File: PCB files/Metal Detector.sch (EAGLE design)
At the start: 125 parts, among them IC1 NE5534AD, IC2 BQ24133RGYR, IC3 LM317MBSTT3, IC4 ESP32-WROOM-32UE-N4, IC5 CP2102, IC6 LM317MBSTT3, J1 L-KLS1-TSJ3.5-013, J2/BATTERY DG128-5.0-02P-14, Q1 IRF740, Q2 BC556, Q3 SI2312CDS-T1-GE3, Q4 MBT3904DW1T1, Q5 SI2312CDS-T1-GE3, Q6 SI2323CDS-T1-GE3, Q7 BC847AE6327HTSA1, T1 BC547, X1 A1944-50, X2 DC21MMX

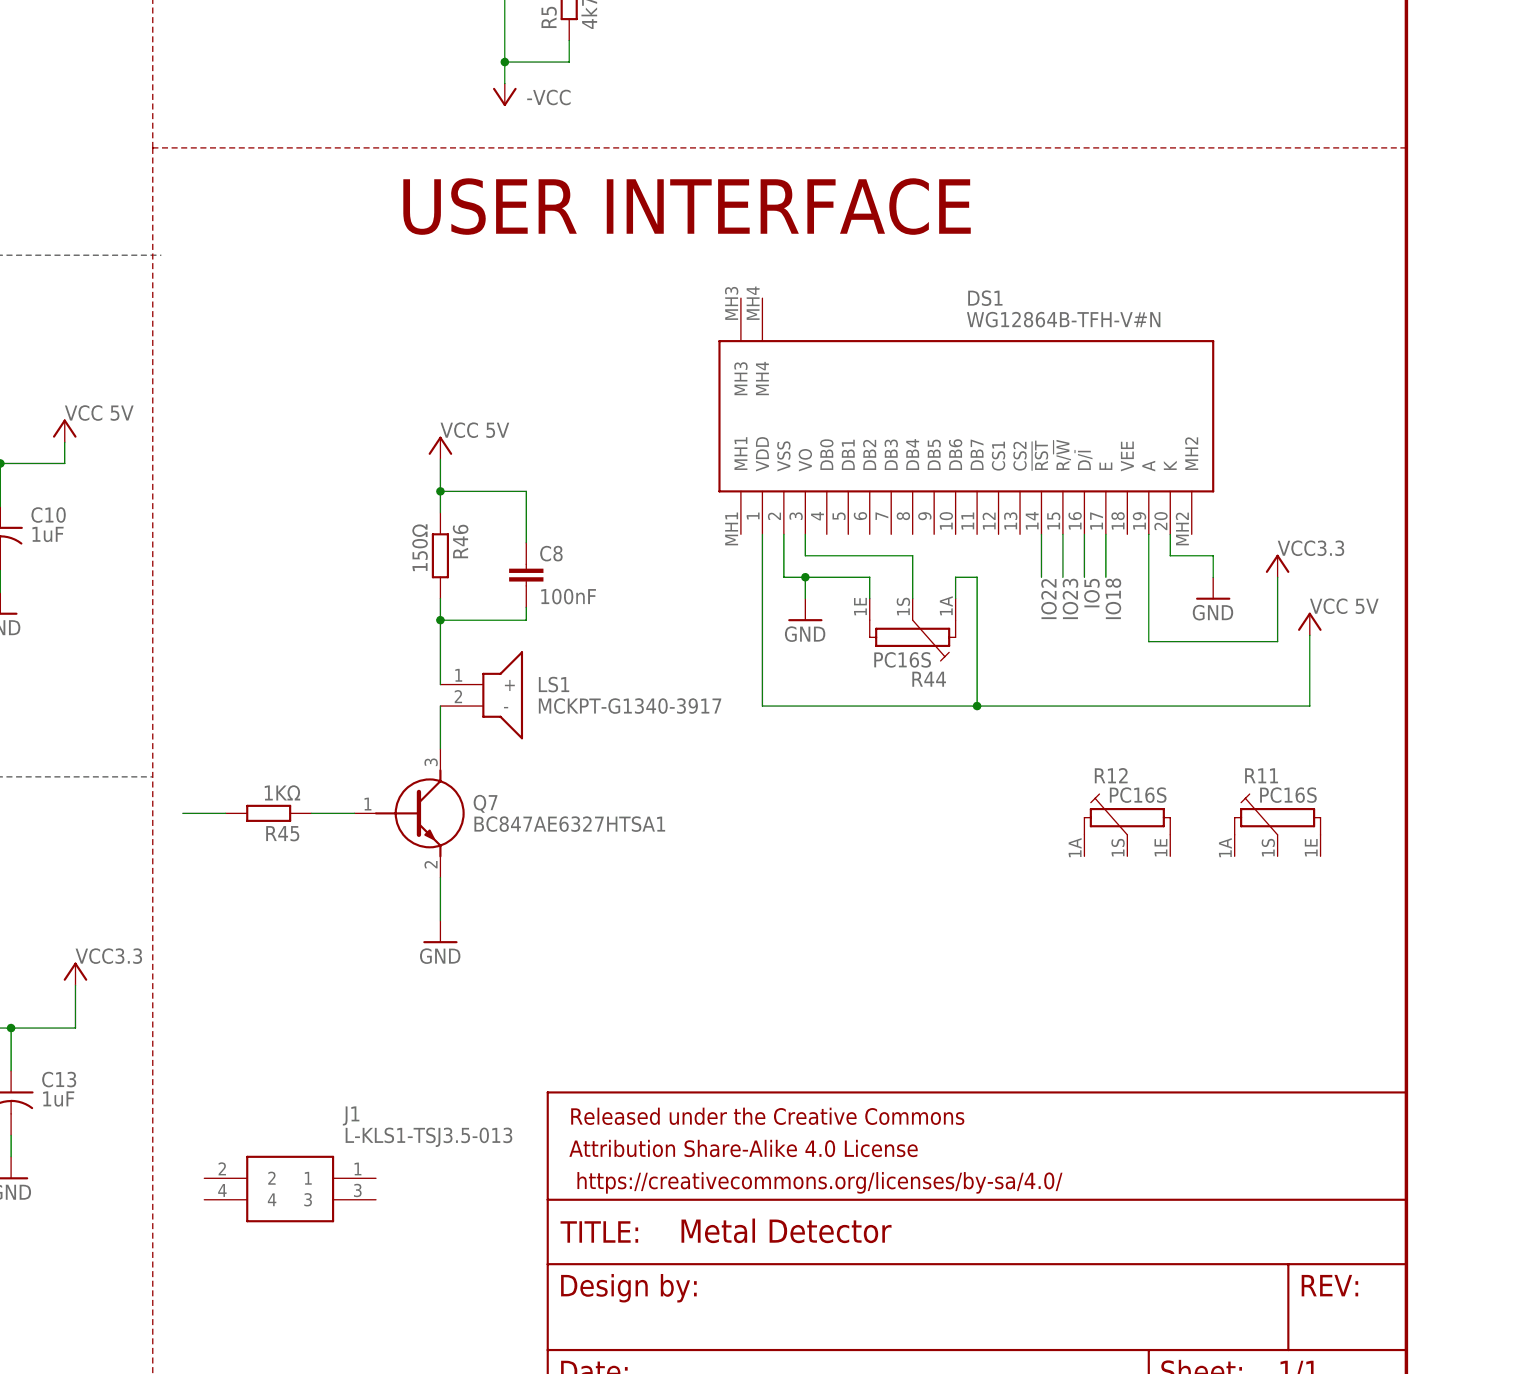
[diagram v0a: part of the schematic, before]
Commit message: Add files via upload
Connected and added Spekers, volume and sensitivty connections with MCU
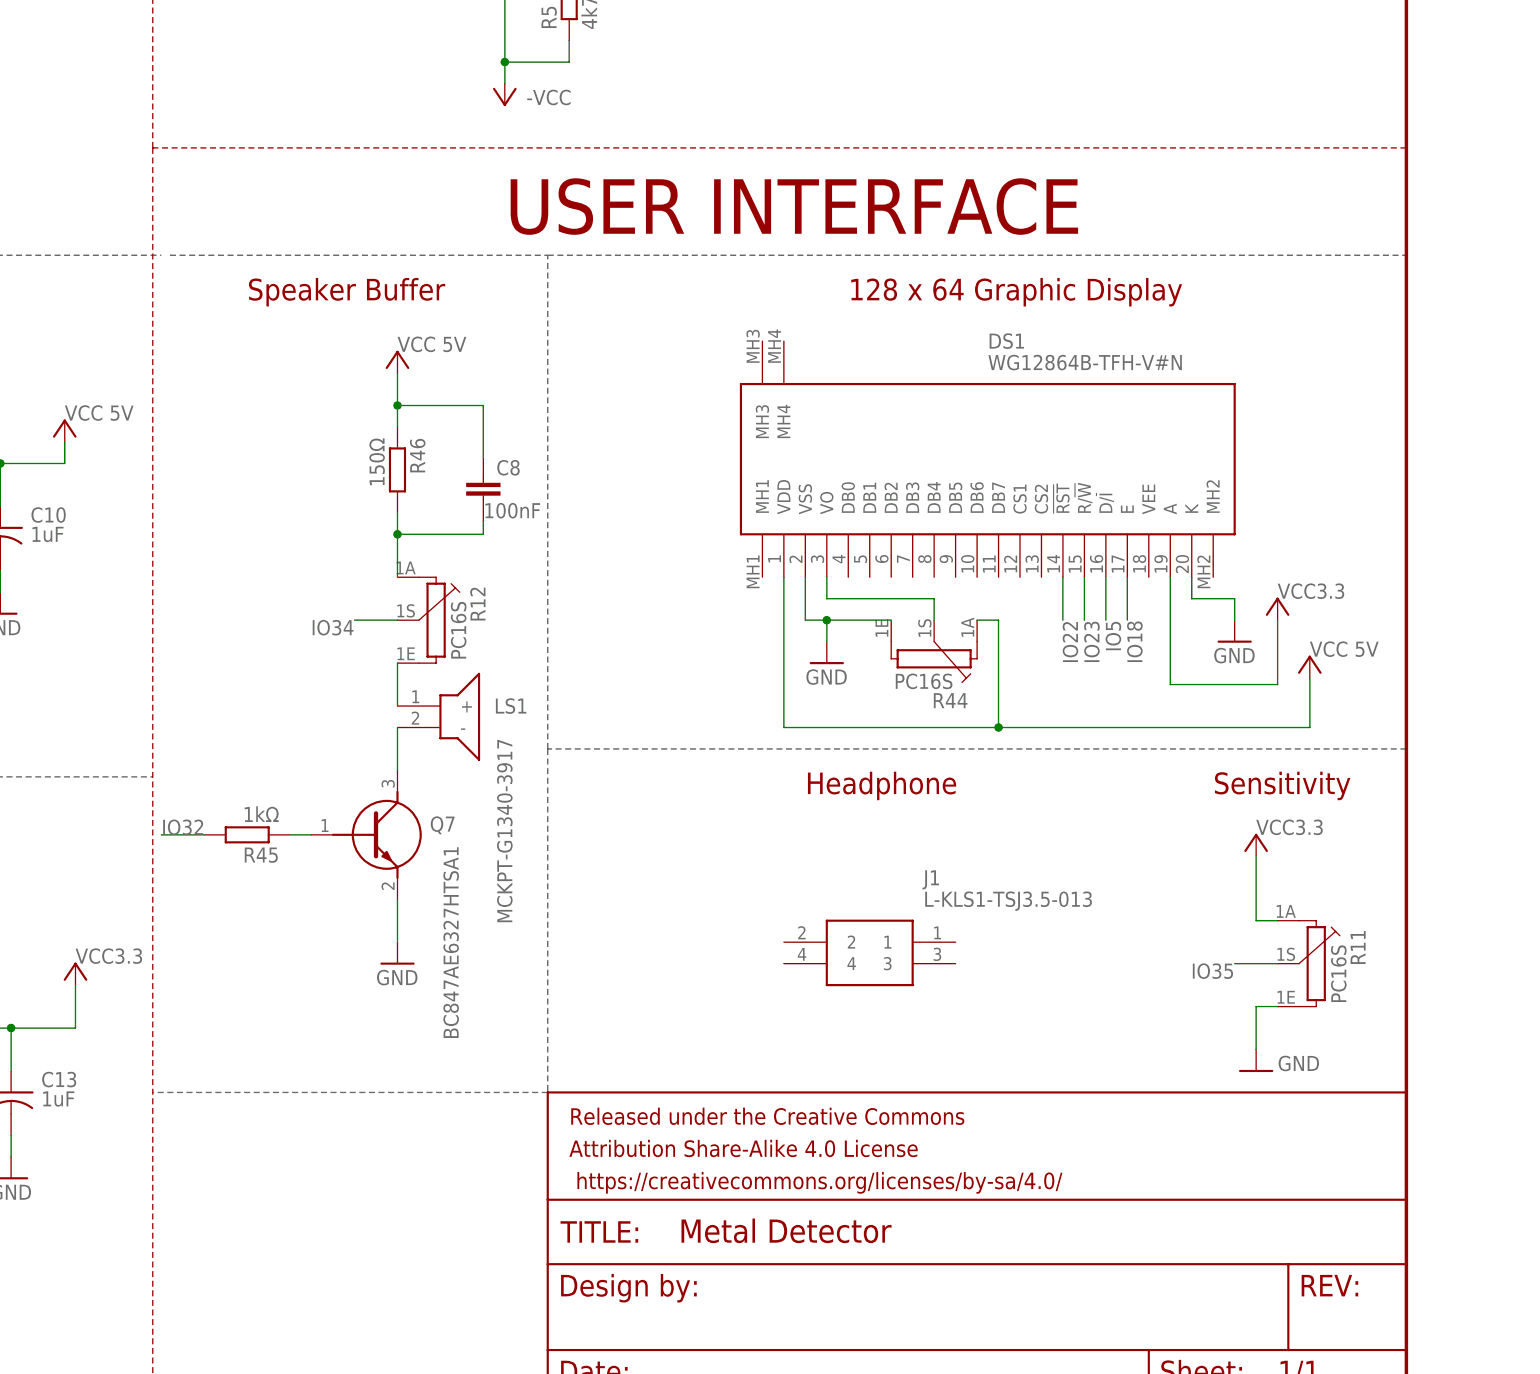
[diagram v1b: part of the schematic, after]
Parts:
- R45: value 1KΩ -> 1kΩ
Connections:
- net GND: now also R11.1E
- net IO32: now also R45.2
- net IO34: now also R12.1S
- net IO35: now also R11.1S
- net N$30: now also R12.1A; no longer LS1.+
- net N$31: now also LS1.+, R12.1E; no longer R45.2
- net VCC: now also R11.1A
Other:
- note added: "128 x 64 Graphic Display"
- note added: "Headphone"
- note added: "Sensitivity"
- note added: "Speaker Buffer"
- moved on the sheet: C8, DS1, J1, LS1, Q7, R11, R12, R44, R45, R46

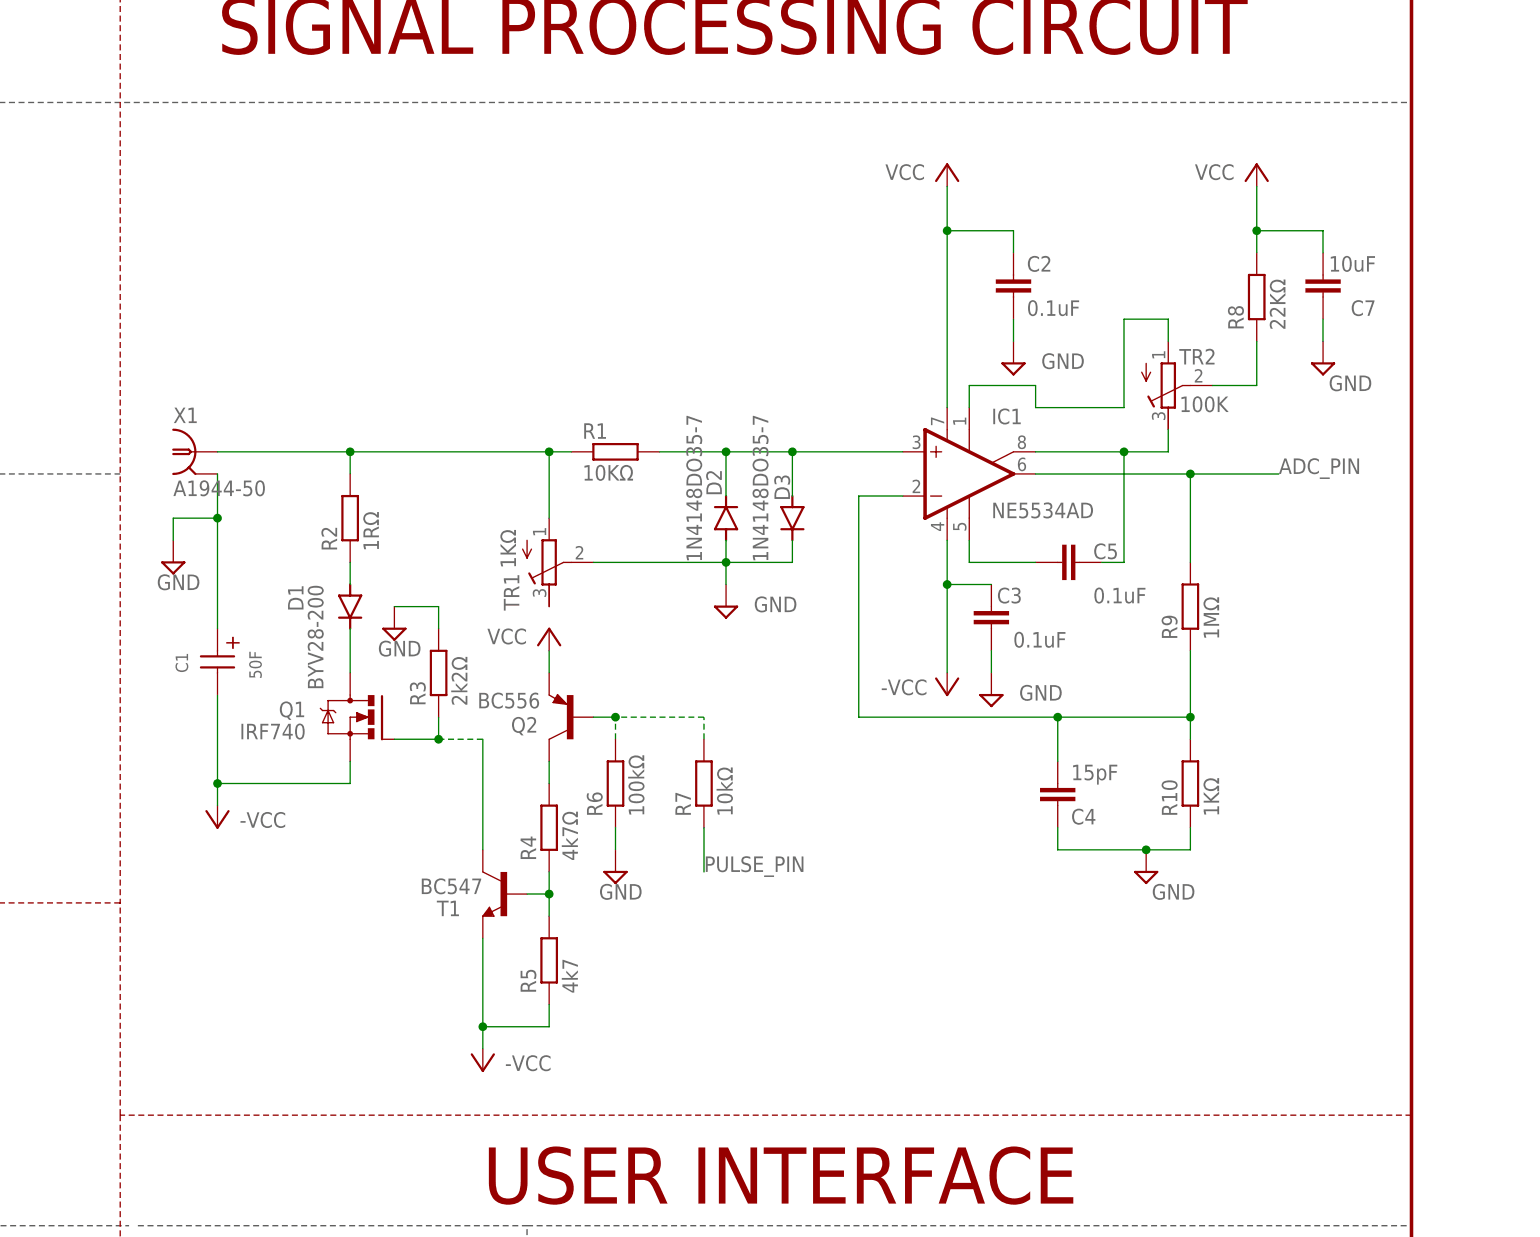
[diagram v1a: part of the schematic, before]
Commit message: Add files via upload
Redesigned signal processing circuit due to ground layer
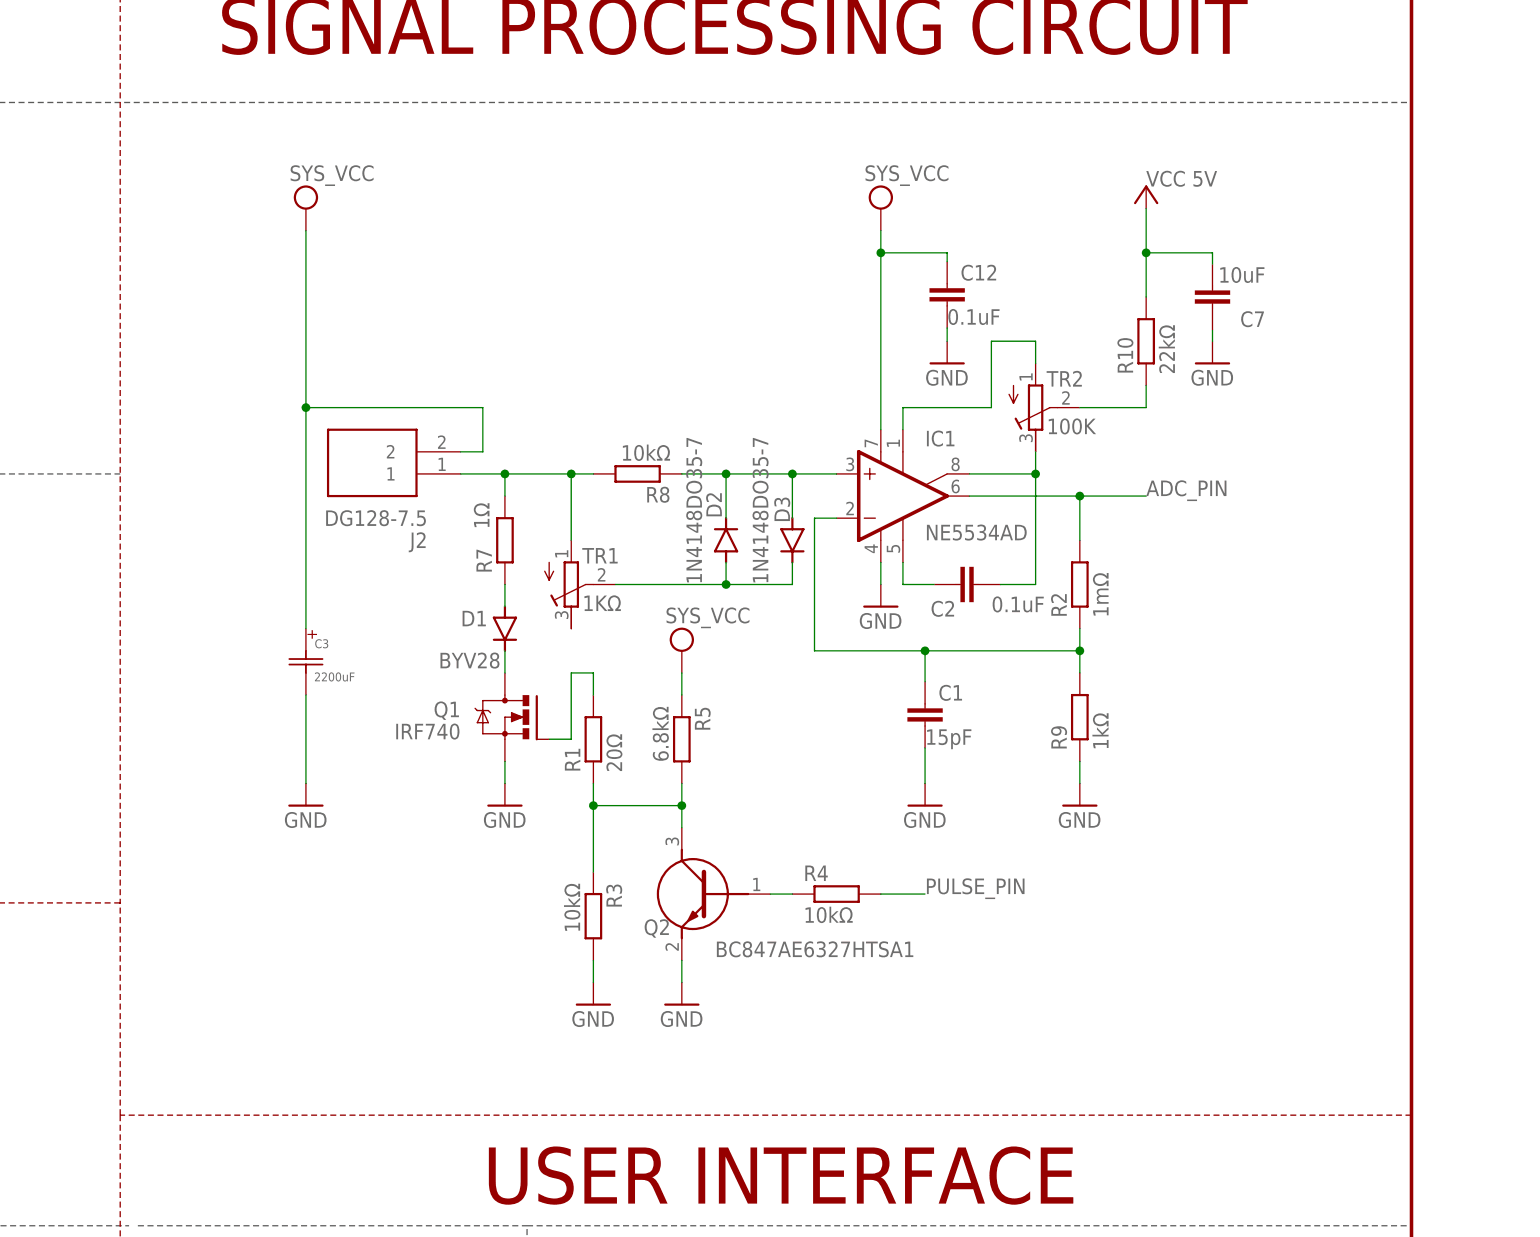
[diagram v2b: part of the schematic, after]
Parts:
- removed C4: 15pF, SparkFun-Capacitors:0.1UF-0402-6.3V-10%-X7R
- removed C5: 0.1uF, SparkFun-Capacitors:0.1UF-0402-6.3V-10%-X7R
- removed R6: 100kΩ, rcl:R-EU_0207/10
- removed T1: BC547, transistor:BC547
- removed X1: A1944-50, con-coax:A1944-50
- added C12: 0.1uF, rcl:C-EUC0603
- added J2: DG128-7.5, DG128-7.5-02P-14-00AH:DG128-7.5-02P-14-00AH
- C1: value 50F -> 15pF; device Wurth_Capacitors_WCAP-STSC:WCAP-STSC_18X40_850617022002 -> rcl:C-EUC0603
- C2: device SparkFun-Capacitors:0.1UF-0402-6.3V-10%-X7R -> rcl:C-EUC0603
- C3: value 0.1uF -> 2200uF; device SparkFun-Capacitors:0.1UF-0402-6.3V-10%-X7R -> 2200uF capacitor:EEUFR1C222
- D1: value BYV28-200 -> BYV28
- Q2: value BC556 -> BC847AE6327HTSA1; device transistor-pnp:BC556 -> BC847AE6327HTSA1:BC847AE6327HTSA1
- R1: value 10KΩ -> 20Ω
- R10: value 1KΩ -> 22kΩ; device rcl:R-EU_0207/10 -> rcl:R-EU_R1206
- R2: value 1RΩ -> 1mΩ; device rcl:R-EU_0207/10 -> rcl:R-EU_R1206
- R3: value 2k2Ω -> 10kΩ
- R4: value 4k7Ω -> 10kΩ
- R5: value 4k7 -> 6.8kΩ; device rcl:R-EU_0207/10 -> rcl:R-EU_R1206
- R7: value 10kΩ -> 1Ω
- R8: value 22KΩ -> 10kΩ
- R9: value 1MΩ -> 1kΩ; device rcl:R-EU_0207/10 -> rcl:R-EU_R1206
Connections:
- removed net N$6 (its old number): R4.1, R5.2, T1.B
- removed net N$8: Q2.B, R6.2, R7.2
- new net N$32: D2.A, D3.C, TR1.S
- new net N$4: D1.A, R7.1
- net ADC_PIN: now also R2.2; no longer R9.2
- net GND: now also C1.2, C12.2, IC1.V-, Q1.S, Q2.E, R9.1; no longer C1.+, C2.2, C4.1, D2.A, D3.C, R10.1, R6.1, TR1.S, X1.2
- net N$1: now also D2.C, D3.A, IC1.+IN, R8.1; no longer R1.1, R2.2, TR1.A, X1.1
- net N$10: now also R10.1; no longer R8.1
- net N$11: now also C2.2; no longer C5.2
- net N$12: now also C1.1, R2.1, R9.2; no longer C4.2, R10.2, R9.1
- net N$13: now also C2.1; no longer C5.1
- net N$2: now also Q1.G; no longer D2.C, D3.A, IC1.+IN
- net N$3: now also Q2.C, R1.1, R3.1, R5.2; no longer D1.A, R2.1
- net N$5: now also Q2.B, R4.1; no longer Q1.G, R3.1, T1.C
- net N$7: now also J2.1, R7.2, R8.2, TR1.A; no longer Q2.C, R4.2
- net PULSE_PIN: now also R4.2; no longer R7.1
- net VCC: now also C12.1, J2.2, R10.2; no longer C1.-, C2.1, IC1.V-, Q1.S, Q2.E, R8.2, T1.E
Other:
- moved on the sheet: C2, C7, D1, D2, D3, IC1, Q1, R1, R10, R2, R3, R4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

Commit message: Add files via upload
Fixed sum bug
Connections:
- removed net N$32: D2.A, D3.C, TR1.S
- net GND: now also D2.A, D3.C, TR1.S
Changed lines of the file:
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@@
 <layer number="59" name="tCarbon" color="7" fill="1" visible="no" active="no"/>
 <layer number="60" name="bCarbon" color="7" fill="1" visible="no" active="no"/>
-<layer number="88" name="SimResults" color="9" fill="1" visible="yes" active="yes"/>
+<layer number="88" name="SimResults" color="9" fill="1" visible="no" active="yes"/>
 <layer number="89" name="SimProbes" color="9" fill="1" visible="yes" active="yes"/>
 <layer number="90" name="Modules" color="5" fill="1" visible="yes" active="yes"/>
@@
 <part name="J2" library="DG128-7.5-02P-14-00AH" deviceset="DG128-7.5-02P-14-00AH" device="" value="DG128-7.5"/>
 <part name="C3" library="2200uF capacitor" deviceset="EEUFR1C222" device="" value="2200uF"/>
+<part name="GND37" library="SparkFun-Aesthetics" deviceset="GND" device=""/>
 </parts>
 <sheets>
@@
 <attribute name="NAME" x="300.7106" y="457.5048" size="1.016" layer="95" ratio="10" rot="SR0"/>
 </instance>
+<instance part="GND37" gate="1" x="347.98" y="457.2" smashed="yes">
+<attribute name="VALUE" x="345.44" y="454.66" size="1.778" layer="96"/>
+</instance>
 </instances>
 <busses>
@@
 <wire x1="299.72" y1="452.12" x2="299.72" y2="441.96" width="0.1524" layer="91"/>
 <pinref part="C3" gate="A" pin="2"/>
+</segment>
+<segment>
+<pinref part="D3" gate="G$1" pin="C"/>
+<wire x1="355.6" y1="467.36" x2="355.6" y2="464.82" width="0.1524" layer="91"/>
+<wire x1="355.6" y1="464.82" x2="347.98" y2="464.82" width="0.1524" layer="91"/>
+<pinref part="D2" gate="G$1" pin="A"/>
+<wire x1="347.98" y1="464.82" x2="347.98" y2="467.36" width="0.1524" layer="91"/>
+<junction x="347.98" y="464.82"/>
+<pinref part="TR1" gate="G$1" pin="S"/>
+<wire x1="335.28" y1="464.82" x2="347.98" y2="464.82" width="0.1524" layer="91"/>
+<pinref part="GND37" gate="1" pin="GND"/>
+<wire x1="347.98" y1="459.74" x2="347.98" y2="464.82" width="0.1524" layer="91"/>
 </segment>
 </net>
@@
 </segment>
 </net>
-<net name="N$32" class="0">
-<segment>
-<pinref part="D3" gate="G$1" pin="C"/>
-<wire x1="355.6" y1="467.36" x2="355.6" y2="464.82" width="0.1524" layer="91"/>
-<wire x1="355.6" y1="464.82" x2="347.98" y2="464.82" width="0.1524" layer="91"/>
-<pinref part="D2" gate="G$1" pin="A"/>
-<wire x1="347.98" y1="464.82" x2="347.98" y2="467.36" width="0.1524" layer="91"/>
-<junction x="347.98" y="464.82"/>
-<pinref part="TR1" gate="G$1" pin="S"/>
-<wire x1="335.28" y1="464.82" x2="347.98" y2="464.82" width="0.1524" layer="91"/>
-</segment>
-</net>
